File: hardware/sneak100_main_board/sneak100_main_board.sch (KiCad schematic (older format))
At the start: 0 parts

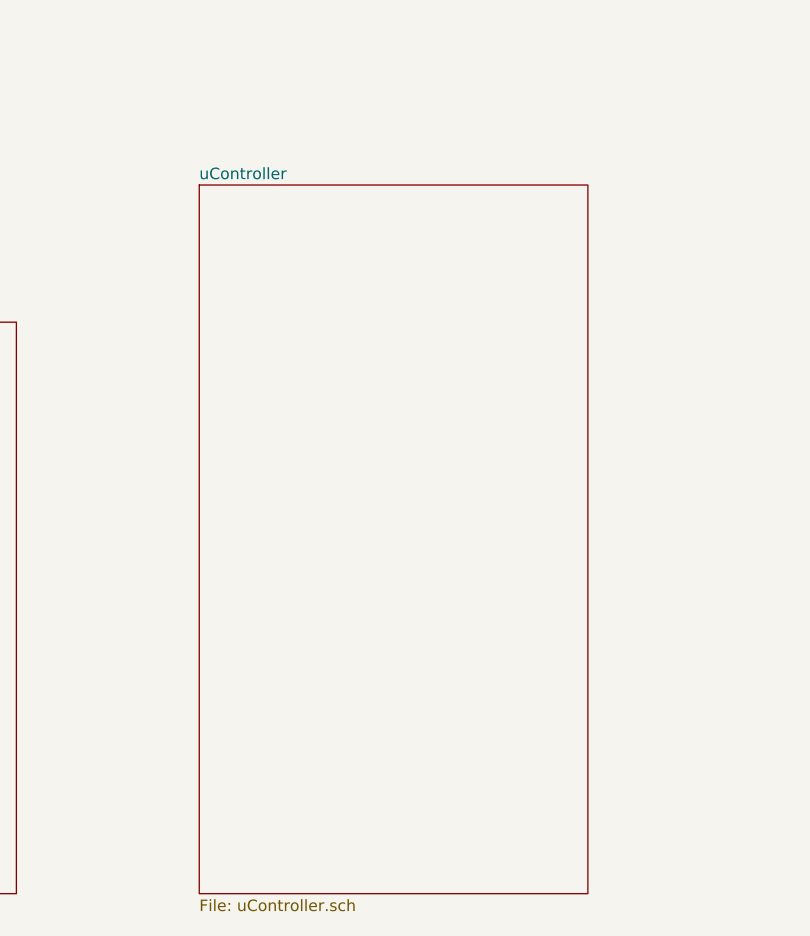
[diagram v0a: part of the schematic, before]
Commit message: User buttons, leds and uart
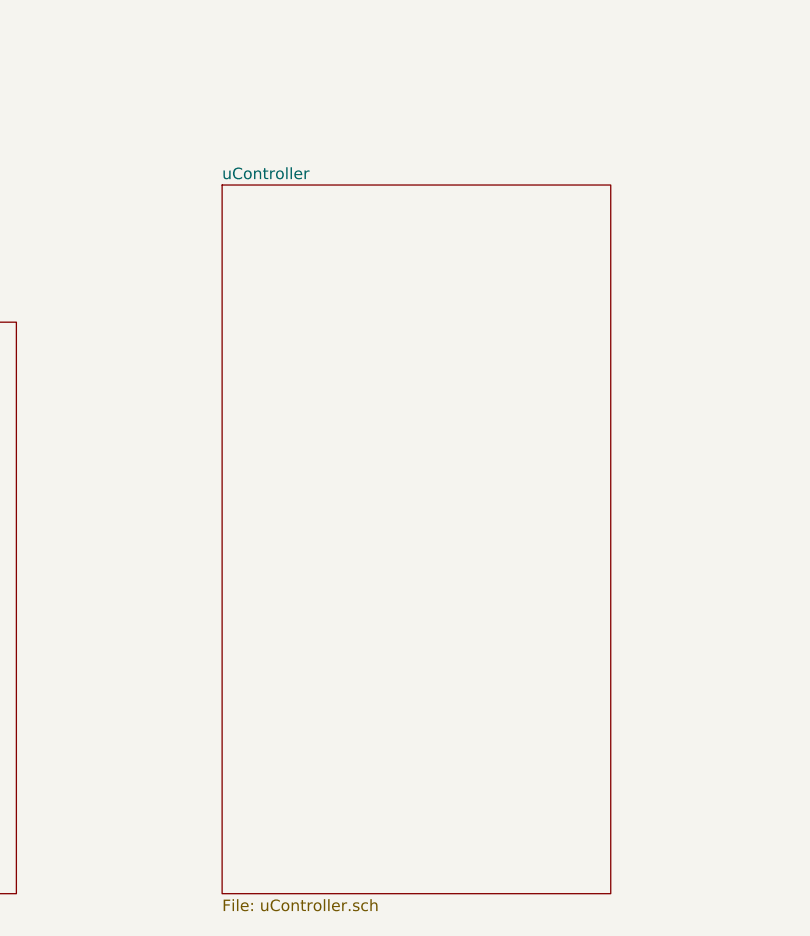
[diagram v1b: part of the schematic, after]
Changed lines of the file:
@@
 $EndDescr
 $Sheet
-S 4650 2900 1700 3100
+S 4750 2900 1700 3100
 U 60E048AE
 F0 "uController" 50

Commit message: motors circuit scheme
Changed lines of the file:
@@
 $EndDescr
 $Sheet
-S 4750 2900 1700 3100
+S 4750 1900 1700 3750
 U 60E048AE
 F0 "uController" 50
@@
 $EndSheet
 $Sheet
-S 2550 3500 1300 2500
+S 2550 3500 1300 2150
 U 60E0491A
 F0 "interface" 50
 F1 "interface.sch" 50
+F2 "BUTTON1" O R 3850 3600 50
+F3 "BUTTON2" O R 3850 3700 50
+F4 "LED1" I R 3850 3900 50
+F5 "LED2" I R 3850 4000 50
+F6 "LED3" I R 3850 4100 50
+F7 "USART1_TX" I R 3850 4300 50
+F8 "USART1_RX" O R 3850 4400 50
 $EndSheet
 $Sheet
-S 7400 2900 1350 950
+S 7400 1900 1350 2000
 U 60E0499A
 F0 "motors" 50
 F1 "motors.sch" 50
+F2 "LF_IN1" I L 7400 2000 50
+F3 "LF_IN2" I L 7400 2100 50
+F4 "LF_A" O L 7400 2200 50
+F5 "LF_B" O L 7400 2300 50
+F6 "RF_IN1" I L 7400 2500 50
+F7 "RF_IN2" I L 7400 2600 50
+F8 "RF_A" O L 7400 2700 50
+F9 "RF_B" O L 7400 2800 50
+F10 "LB_IN1" I L 7400 3000 50
+F11 "LB_IN2" I L 7400 3100 50
+F12 "LB_A" O L 7400 3200 50
+F13 "LB_B" O L 7400 3300 50
+F14 "RB_IN1" I L 7400 3500 50
+F15 "RB_IN2" I L 7400 3600 50
+F16 "RB_A" O L 7400 3700 50
+F17 "RB_B" O L 7400 3800 50
 $EndSheet
 $Sheet
-S 1050 1000 1500 1100
+S 2550 1900 1300 1100
 U 60E04AFA
 F0 "power" 50
@@
 $EndSheet
 $Sheet
-S 7400 4200 1350 1000
+S 7400 4200 1350 600
 U 60E049FE
 F0 "proximitySensors" 50
 F1 "proximitySensors.sch" 50
-F2 "TX_ADD0" I L 7400 4300 50
-F3 "TX_ADD1" I L 7400 4400 50
-F4 "TX_ADD2" I L 7400 4500 50
-F5 "RX_ADD0" I L 7400 4800 50
-F6 "RX_ADD1" I L 7400 4900 50
-F7 "RX_ADD2" I L 7400 5000 50
-F8 "RX_READ" O L 7400 5100 50
-F9 "TX_ENABLE" I L 7400 4600 50
+F2 "RX_READ" O L 7400 4700 50
+F3 "TX_ENABLE" I L 7400 4600 50
+F4 "ADD0" I L 7400 4300 50
+F5 "ADD1" I L 7400 4400 50
+F6 "ADD2" I L 7400 4500 50
 $EndSheet
 $Sheet
-S 7400 5500 1350 500
+S 7400 5150 1350 500
 U 60E04A74
 F0 "lineSensors" 50
 F1 "lineSennsors.sch" 50
-F2 "READ_LL" O L 7400 5600 50
-F3 "READ_LM" O L 7400 5700 50
-F4 "READ_RM" O L 7400 5800 50
-F5 "READ_RR" O L 7400 5900 50
+F2 "READ_LL" O L 7400 5250 50
+F3 "READ_LM" O L 7400 5350 50
+F4 "READ_RM" O L 7400 5450 50
+F5 "READ_RR" O L 7400 5550 50
 $EndSheet
 $EndSCHEMATC

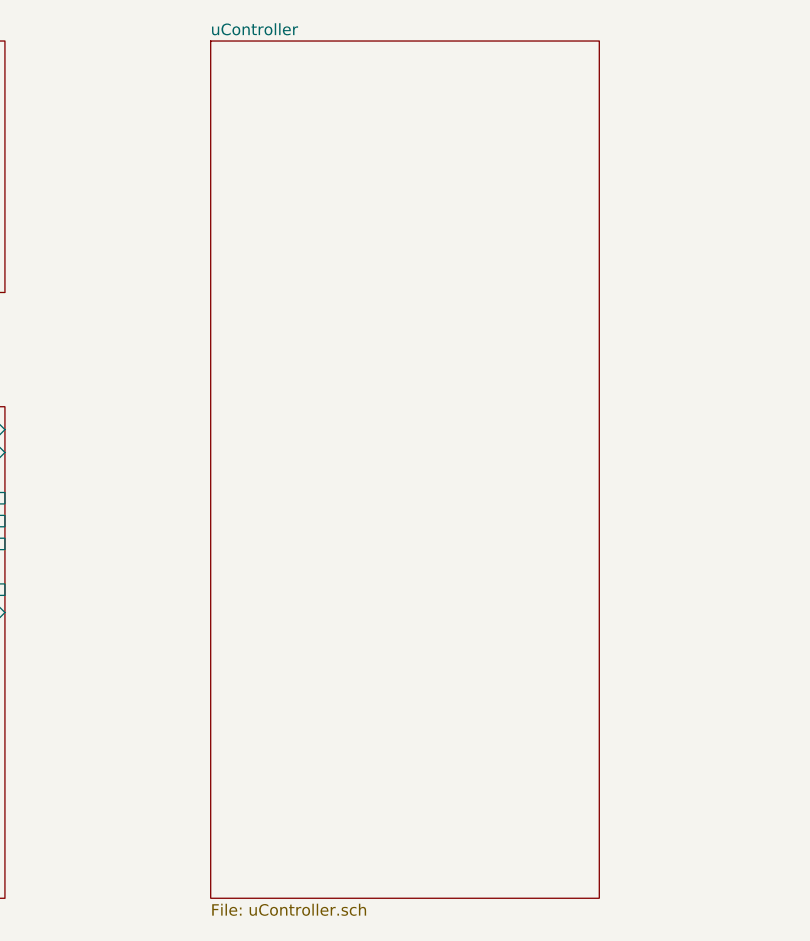
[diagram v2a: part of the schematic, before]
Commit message: Add stm32f405 uC scheme
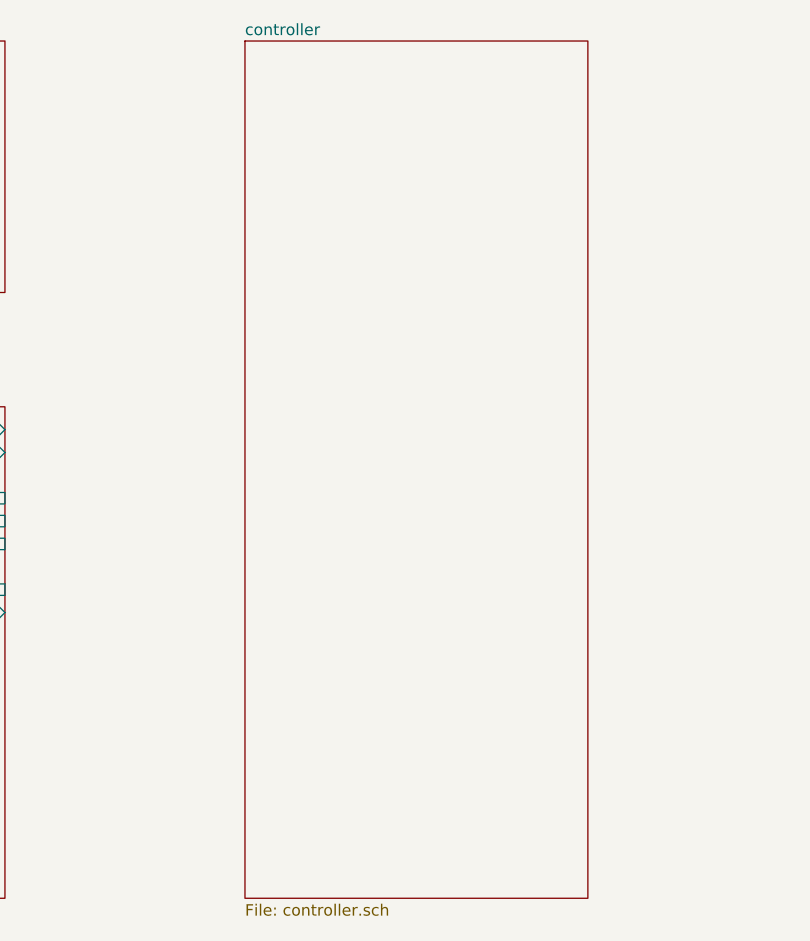
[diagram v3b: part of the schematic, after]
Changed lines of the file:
@@
 $EndDescr
-$Sheet
-S 4750 1900 1700 3750
-U 60E048AE
-F0 "uController" 50
-F1 "uController.sch" 50
-$EndSheet
 $Sheet
 S 2550 3500 1300 2150
@@
 F5 "READ_RR" O L 7400 5550 50
 $EndSheet
+$Sheet
+S 4900 1900 1500 3750
+U 6100FE40
+F0 "controller" 50
+F1 "controller.sch" 50
+$EndSheet
 $EndSCHEMATC

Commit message: Hardware configuration schematic
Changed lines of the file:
@@
 $EndDescr
 $Sheet
-S 2550 3500 1300 2150
+S 3150 3500 1300 2150
 U 60E0491A
 F0 "interface" 50
 F1 "interface.sch" 50
-F2 "BUTTON1" O R 3850 3600 50
-F3 "BUTTON2" O R 3850 3700 50
-F4 "LED1" I R 3850 3900 50
-F5 "LED2" I R 3850 4000 50
-F6 "LED3" I R 3850 4100 50
-F7 "USART1_TX" I R 3850 4300 50
-F8 "USART1_RX" O R 3850 4400 50
+F2 "BUTTON1" O R 4450 3600 50
+F3 "BUTTON2" O R 4450 3700 50
+F4 "LED1" I R 4450 3900 50
+F5 "LED2" I R 4450 4000 50
+F6 "LED3" I R 4450 4100 50
+F7 "USB_DP" B R 4450 5000 50
+F8 "USB_DM" B R 4450 4900 50
+F9 "BLUETOOTH_RX" I R 4450 4300 50
+F10 "BLUETOOTH_TX" O R 4450 4400 50
+F11 "I2C_SDA" B R 4450 4700 50
+F12 "I2C_SCL" B R 4450 4600 50
+F13 "MODULE_START" O R 4450 5400 50
+F14 "MODULE_KILL" O R 4450 5500 50
+F15 "RECEIVER_OUT" O R 4450 5200 50
 $EndSheet
 $Sheet
-S 7400 1900 1350 2000
+S 6900 1900 1350 2000
 U 60E0499A
 F0 "motors" 50
 F1 "motors.sch" 50
-F2 "LF_IN1" I L 7400 2000 50
-F3 "LF_IN2" I L 7400 2100 50
-F4 "LF_A" O L 7400 2200 50
-F5 "LF_B" O L 7400 2300 50
-F6 "RF_IN1" I L 7400 2500 50
-F7 "RF_IN2" I L 7400 2600 50
-F8 "RF_A" O L 7400 2700 50
-F9 "RF_B" O L 7400 2800 50
-F10 "LB_IN1" I L 7400 3000 50
-F11 "LB_IN2" I L 7400 3100 50
-F12 "LB_A" O L 7400 3200 50
-F13 "LB_B" O L 7400 3300 50
-F14 "RB_IN1" I L 7400 3500 50
-F15 "RB_IN2" I L 7400 3600 50
-F16 "RB_A" O L 7400 3700 50
-F17 "RB_B" O L 7400 3800 50
+F2 "LF_IN1" I L 6900 2000 50
+F3 "LF_IN2" I L 6900 2100 50
+F4 "LF_A" O L 6900 2200 50
+F5 "LF_B" O L 6900 2300 50
+F6 "RF_IN1" I L 6900 2500 50
+F7 "RF_IN2" I L 6900 2600 50
+F8 "RF_A" O L 6900 2700 50
+F9 "RF_B" O L 6900 2800 50
+F10 "LB_IN1" I L 6900 3000 50
+F11 "LB_IN2" I L 6900 3100 50
+F12 "LB_A" O L 6900 3200 50
+F13 "LB_B" O L 6900 3300 50
+F14 "RB_IN1" I L 6900 3500 50
+F15 "RB_IN2" I L 6900 3600 50
+F16 "RB_A" O L 6900 3700 50
+F17 "RB_B" O L 6900 3800 50
 $EndSheet
 $Sheet
-S 2550 1900 1300 1100
+S 3150 1900 1300 1100
 U 60E04AFA
 F0 "power" 50
@@
 $EndSheet
 $Sheet
-S 7400 4200 1350 600
+S 6900 4200 1350 600
 U 60E049FE
 F0 "proximitySensors" 50
 F1 "proximitySensors.sch" 50
-F2 "RX_READ" O L 7400 4700 50
-F3 "TX_ENABLE" I L 7400 4600 50
-F4 "ADD0" I L 7400 4300 50
-F5 "ADD1" I L 7400 4400 50
-F6 "ADD2" I L 7400 4500 50
+F2 "RX_READ" O L 6900 4700 50
+F3 "TX_ENABLE" I L 6900 4600 50
+F4 "ADD0" I L 6900 4300 50
+F5 "ADD1" I L 6900 4400 50
+F6 "ADD2" I L 6900 4500 50
 $EndSheet
 $Sheet
-S 7400 5150 1350 500
+S 6900 5150 1350 500
 U 60E04A74
 F0 "lineSensors" 50
 F1 "lineSennsors.sch" 50
-F2 "READ_LL" O L 7400 5250 50
-F3 "READ_LM" O L 7400 5350 50
-F4 "READ_RM" O L 7400 5450 50
-F5 "READ_RR" O L 7400 5550 50
+F2 "READ_LL" O L 6900 5250 50
+F3 "READ_LM" O L 6900 5350 50
+F4 "READ_RM" O L 6900 5450 50
+F5 "READ_RR" O L 6900 5550 50
 $EndSheet
 $Sheet
@@
 F0 "controller" 50
 F1 "controller.sch" 50
+F2 "RESET" I L 4900 3700 50
+F3 "RF_A" I R 6400 2700 50
+F4 "RF_B" I R 6400 2800 50
+F5 "USART2_TX" O L 4900 4300 50
+F6 "USART2_RX" I L 4900 4400 50
+F7 "LB_A" I R 6400 3200 50
+F8 "LB_B" I R 6400 3300 50
+F9 "I2C3_SCL" B L 4900 4600 50
+F10 "USB_DM" B L 4900 4900 50
+F11 "USB_DP" B L 4900 5000 50
+F12 "USER_LED1" O L 4900 3900 50
+F13 "LB_IN1" O R 6400 3000 50
+F14 "LB_IN2" O R 6400 3100 50
+F15 "PROXIMITY_ADD0" O R 6400 4300 50
+F16 "PROXIMITY_ADD1" O R 6400 4400 50
+F17 "PROXIMITY_ADD2" O R 6400 4500 50
+F18 "RB_A" I R 6400 3700 50
+F19 "RB_B" I R 6400 3800 50
+F20 "RB_IN1" O R 6400 3500 50
+F21 "RB_IN2" O R 6400 3600 50
+F22 "RF_IN1" O R 6400 2500 50
+F23 "RF_IN2" O R 6400 2600 50
+F24 "LF_IN1" O R 6400 2000 50
+F25 "LF_IN2" O R 6400 2100 50
+F26 "LINE_LL" I R 6400 5250 50
+F27 "LINE_LM" I R 6400 5350 50
+F28 "LINE_RM" I R 6400 5450 50
+F29 "LINE_RR" I R 6400 5550 50
+F30 "BATTERY_SENSE" I L 4900 2450 50
+F31 "PROXIMITY_RX_READ" I R 6400 4700 50
+F32 "LF_A" I R 6400 2200 50
+F33 "LF_B" I R 6400 2300 50
+F34 "PROXIMITY_TX_ENABLE" O R 6400 4600 50
+F35 "I2C3_SDA" B L 4900 4700 50
+F36 "USER_LED2" O L 4900 4000 50
+F37 "USER_LED3" O L 4900 4100 50
+F38 "USER_BUTTON" I L 4900 3600 50
+F39 "MODULE_START" I L 4900 5400 50
+F40 "MODULE_KILL" I L 4900 5500 50
+F41 "RECEIVER_OUT" I L 4900 5200 50
 $EndSheet
+Wire Wire Line
+	6400 2000 6900 2000
+Wire Wire Line
+	6400 2100 6900 2100
+Wire Wire Line
+	6400 2200 6900 2200
+Wire Wire Line
+	6400 2300 6900 2300
+Wire Wire Line
+	6400 2500 6900 2500
+Wire Wire Line
+	6400 2600 6900 2600
+Wire Wire Line
+	6400 2700 6900 2700
+Wire Wire Line
+	6400 2800 6900 2800
+Wire Wire Line
+	6400 3000 6900 3000
+Wire Wire Line
+	6400 3100 6900 3100
+Wire Wire Line
+	6400 3200 6900 3200
+Wire Wire Line
+	6400 3300 6900 3300
+Wire Wire Line
+	6400 3500 6900 3500
+Wire Wire Line
+	6400 3600 6900 3600
+Wire Wire Line
+	6400 3700 6900 3700
+Wire Wire Line
+	6400 3800 6900 3800
+Wire Wire Line
+	6400 4300 6900 4300
+Wire Wire Line
+	6400 4400 6900 4400
+Wire Wire Line
+	6400 4500 6900 4500
+Wire Wire Line
+	6400 4600 6900 4600
+Wire Wire Line
+	6400 4700 6900 4700
+Wire Wire Line
+	6400 5250 6900 5250
+Wire Wire Line
+	6400 5350 6900 5350
+Wire Wire Line
+	6400 5450 6900 5450
+Wire Wire Line
+	6400 5550 6900 5550
+Wire Wire Line
+	4450 3600 4900 3600
+Wire Wire Line
+	4450 3700 4900 3700
+Wire Wire Line
+	4450 3900 4900 3900
+Wire Wire Line
+	4450 4000 4900 4000
+Wire Wire Line
+	4450 4100 4900 4100
+Wire Wire Line
+	4900 4900 4450 4900
+Wire Wire Line
+	4900 5000 4450 5000
+Wire Wire Line
+	4900 4300 4450 4300
+Wire Wire Line
+	4900 4400 4450 4400
+Wire Wire Line
+	4900 4600 4450 4600
+Wire Wire Line
+	4900 4700 4450 4700
+Wire Wire Line
+	4450 5400 4900 5400
+Wire Wire Line
+	4450 5500 4900 5500
+Wire Wire Line
+	4450 5200 4900 5200
 $EndSCHEMATC

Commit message: Power section scheme
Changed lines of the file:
@@
 F0 "power" 50
 F1 "power.sch" 50
+F2 "BATTERY_SENSE" O R 4450 2450 50
 $EndSheet
 $Sheet
@@
 Wire Wire Line
 	4450 5200 4900 5200
+Wire Wire Line
+	4450 2450 4900 2450
 $EndSCHEMATC

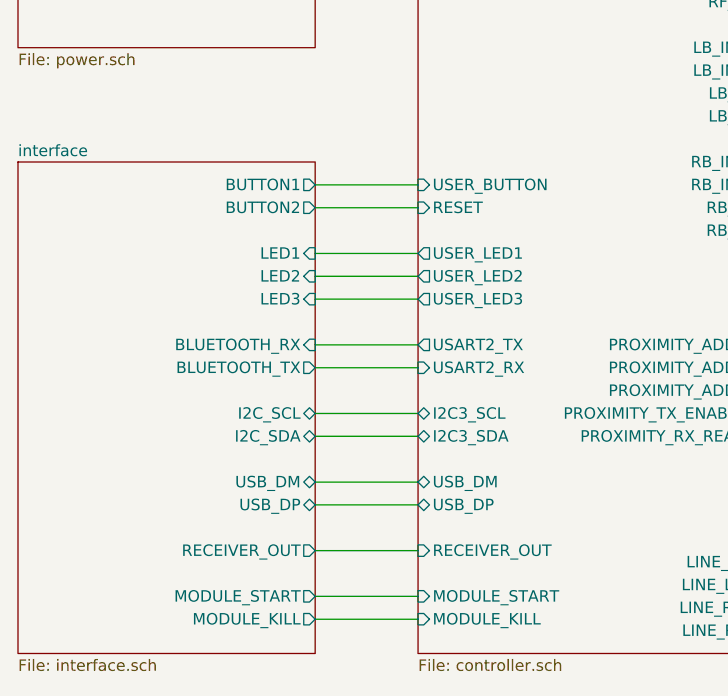
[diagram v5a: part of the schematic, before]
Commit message: USB FDU mode
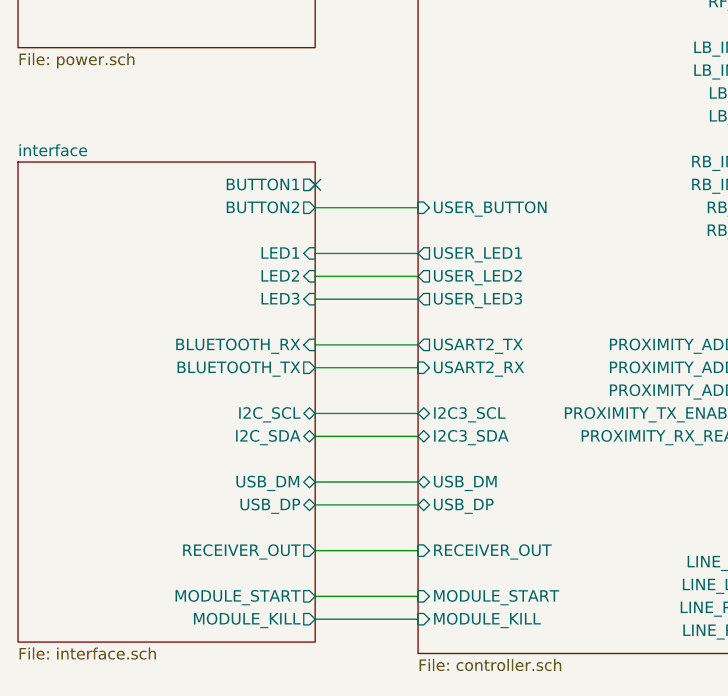
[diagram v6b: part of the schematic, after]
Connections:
- no-connect marks 0 -> 1
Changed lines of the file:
@@
 $EndDescr
-$Sheet
-S 3150 3500 1300 2150
-U 60E0491A
-F0 "interface" 50
-F1 "interface.sch" 50
-F2 "BUTTON1" O R 4450 3600 50
-F3 "BUTTON2" O R 4450 3700 50
-F4 "LED1" I R 4450 3900 50
-F5 "LED2" I R 4450 4000 50
-F6 "LED3" I R 4450 4100 50
-F7 "USB_DP" B R 4450 5000 50
-F8 "USB_DM" B R 4450 4900 50
-F9 "BLUETOOTH_RX" I R 4450 4300 50
-F10 "BLUETOOTH_TX" O R 4450 4400 50
-F11 "I2C_SDA" B R 4450 4700 50
-F12 "I2C_SCL" B R 4450 4600 50
-F13 "MODULE_START" O R 4450 5400 50
-F14 "MODULE_KILL" O R 4450 5500 50
-F15 "RECEIVER_OUT" O R 4450 5200 50
-$EndSheet
 $Sheet
 S 6900 1900 1350 2000
@@
 F4 "READ_RM" O L 6900 5450 50
 F5 "READ_RR" O L 6900 5550 50
-$EndSheet
-$Sheet
-S 4900 1900 1500 3750
-U 6100FE40
-F0 "controller" 50
-F1 "controller.sch" 50
-F2 "RESET" I L 4900 3700 50
-F3 "RF_A" I R 6400 2700 50
-F4 "RF_B" I R 6400 2800 50
-F5 "USART2_TX" O L 4900 4300 50
-F6 "USART2_RX" I L 4900 4400 50
-F7 "LB_A" I R 6400 3200 50
-F8 "LB_B" I R 6400 3300 50
-F9 "I2C3_SCL" B L 4900 4600 50
-F10 "USB_DM" B L 4900 4900 50
-F11 "USB_DP" B L 4900 5000 50
-F12 "USER_LED1" O L 4900 3900 50
-F13 "LB_IN1" O R 6400 3000 50
-F14 "LB_IN2" O R 6400 3100 50
-F15 "PROXIMITY_ADD0" O R 6400 4300 50
-F16 "PROXIMITY_ADD1" O R 6400 4400 50
-F17 "PROXIMITY_ADD2" O R 6400 4500 50
-F18 "RB_A" I R 6400 3700 50
-F19 "RB_B" I R 6400 3800 50
-F20 "RB_IN1" O R 6400 3500 50
-F21 "RB_IN2" O R 6400 3600 50
-F22 "RF_IN1" O R 6400 2500 50
-F23 "RF_IN2" O R 6400 2600 50
-F24 "LF_IN1" O R 6400 2000 50
-F25 "LF_IN2" O R 6400 2100 50
-F26 "LINE_LL" I R 6400 5250 50
-F27 "LINE_LM" I R 6400 5350 50
-F28 "LINE_RM" I R 6400 5450 50
-F29 "LINE_RR" I R 6400 5550 50
-F30 "BATTERY_SENSE" I L 4900 2450 50
-F31 "PROXIMITY_RX_READ" I R 6400 4700 50
-F32 "LF_A" I R 6400 2200 50
-F33 "LF_B" I R 6400 2300 50
-F34 "PROXIMITY_TX_ENABLE" O R 6400 4600 50
-F35 "I2C3_SDA" B L 4900 4700 50
-F36 "USER_LED2" O L 4900 4000 50
-F37 "USER_LED3" O L 4900 4100 50
-F38 "USER_BUTTON" I L 4900 3600 50
-F39 "MODULE_START" I L 4900 5400 50
-F40 "MODULE_KILL" I L 4900 5500 50
-F41 "RECEIVER_OUT" I L 4900 5200 50
 $EndSheet
 Wire Wire Line
@@
 	6400 5550 6900 5550
 Wire Wire Line
-	4450 3600 4900 3600
-Wire Wire Line
 	4450 3700 4900 3700
 Wire Wire Line
@@
 Wire Wire Line
 	4450 2450 4900 2450
+$Sheet
+S 3150 3500 1300 2100
+U 60E0491A
+F0 "interface" 50
+F1 "interface.sch" 50
+F2 "BUTTON1" O R 4450 3600 50
+F3 "BUTTON2" O R 4450 3700 50
+F4 "LED1" I R 4450 3900 50
+F5 "LED2" I R 4450 4000 50
+F6 "LED3" I R 4450 4100 50
+F7 "USB_DP" B R 4450 5000 50
+F8 "USB_DM" B R 4450 4900 50
+F9 "BLUETOOTH_RX" I R 4450 4300 50
+F10 "BLUETOOTH_TX" O R 4450 4400 50
+F11 "I2C_SDA" B R 4450 4700 50
+F12 "I2C_SCL" B R 4450 4600 50
+F13 "MODULE_START" O R 4450 5400 50
+F14 "MODULE_KILL" O R 4450 5500 50
+F15 "RECEIVER_OUT" O R 4450 5200 50
+$EndSheet
+$Sheet
+S 4900 1900 1500 3750
+U 6100FE40
+F0 "controller" 50
+F1 "controller.sch" 50
+F2 "RF_A" I R 6400 2700 50
+F3 "RF_B" I R 6400 2800 50
+F4 "USART2_TX" O L 4900 4300 50
+F5 "USART2_RX" I L 4900 4400 50
+F6 "LB_A" I R 6400 3200 50
+F7 "LB_B" I R 6400 3300 50
+F8 "I2C3_SCL" B L 4900 4600 50
+F9 "USB_DM" B L 4900 4900 50
+F10 "USB_DP" B L 4900 5000 50
+F11 "USER_LED1" O L 4900 3900 50
+F12 "LB_IN1" O R 6400 3000 50
+F13 "LB_IN2" O R 6400 3100 50
+F14 "PROXIMITY_ADD0" O R 6400 4300 50
+F15 "PROXIMITY_ADD1" O R 6400 4400 50
+F16 "PROXIMITY_ADD2" O R 6400 4500 50
+F17 "RB_A" I R 6400 3700 50
+F18 "RB_B" I R 6400 3800 50
+F19 "RB_IN1" O R 6400 3500 50
+F20 "RB_IN2" O R 6400 3600 50
+F21 "RF_IN1" O R 6400 2500 50
+F22 "RF_IN2" O R 6400 2600 50
+F23 "LF_IN1" O R 6400 2000 50
+F24 "LF_IN2" O R 6400 2100 50
+F25 "LINE_LL" I R 6400 5250 50
+F26 "LINE_LM" I R 6400 5350 50
+F27 "LINE_RM" I R 6400 5450 50
+F28 "LINE_RR" I R 6400 5550 50
+F29 "BATTERY_SENSE" I L 4900 2450 50
+F30 "PROXIMITY_RX_READ" I R 6400 4700 50
+F31 "LF_A" I R 6400 2200 50
+F32 "LF_B" I R 6400 2300 50
+F33 "PROXIMITY_TX_ENABLE" O R 6400 4600 50
+F34 "I2C3_SDA" B L 4900 4700 50
+F35 "USER_LED2" O L 4900 4000 50
+F36 "USER_LED3" O L 4900 4100 50
+F37 "USER_BUTTON" I L 4900 3700 50
+F38 "MODULE_START" I L 4900 5400 50
+F39 "MODULE_KILL" I L 4900 5500 50
+F40 "RECEIVER_OUT" I L 4900 5200 50
+$EndSheet
+NoConn ~ 4450 3600
 $EndSCHEMATC

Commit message: Layout progress
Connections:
- no-connect marks 1 -> 0
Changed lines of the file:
@@
 	4900 4700 4450 4700
-Wire Wire Line
-	4450 5400 4900 5400
-Wire Wire Line
-	4450 5500 4900 5500
 Wire Wire Line
 	4450 5200 4900 5200
@@
 F0 "interface" 50
 F1 "interface.sch" 50
-F2 "BUTTON1" O R 4450 3600 50
-F3 "BUTTON2" O R 4450 3700 50
-F4 "LED1" I R 4450 3900 50
-F5 "LED2" I R 4450 4000 50
-F6 "LED3" I R 4450 4100 50
-F7 "USB_DP" B R 4450 5000 50
-F8 "USB_DM" B R 4450 4900 50
-F9 "BLUETOOTH_RX" I R 4450 4300 50
-F10 "BLUETOOTH_TX" O R 4450 4400 50
-F11 "I2C_SDA" B R 4450 4700 50
-F12 "I2C_SCL" B R 4450 4600 50
-F13 "MODULE_START" O R 4450 5400 50
-F14 "MODULE_KILL" O R 4450 5500 50
-F15 "RECEIVER_OUT" O R 4450 5200 50
+F2 "LED1" I R 4450 3900 50
+F3 "LED2" I R 4450 4000 50
+F4 "LED3" I R 4450 4100 50
+F5 "USB_DP" B R 4450 5000 50
+F6 "USB_DM" B R 4450 4900 50
+F7 "BLUETOOTH_RX" I R 4450 4300 50
+F8 "BLUETOOTH_TX" O R 4450 4400 50
+F9 "I2C_SDA" B R 4450 4700 50
+F10 "I2C_SCL" B R 4450 4600 50
+F11 "RECEIVER_OUT" O R 4450 5200 50
+F12 "BUTTON" O R 4450 3700 50
 $EndSheet
 $Sheet
@@
 F36 "USER_LED3" O L 4900 4100 50
 F37 "USER_BUTTON" I L 4900 3700 50
-F38 "MODULE_START" I L 4900 5400 50
-F39 "MODULE_KILL" I L 4900 5500 50
-F40 "RECEIVER_OUT" I L 4900 5200 50
+F38 "RECEIVER_OUT" I L 4900 5200 50
 $EndSheet
-NoConn ~ 4450 3600
 $EndSCHEMATC
